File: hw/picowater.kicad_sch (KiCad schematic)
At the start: 45 parts, among them J1 +12V, J10 Batt TP, J11 Humidity, J12 Ultrasound, J2 Power In, J3 +5V Pins, J4 UART, J5 Power Out, J6 JST-PH2 Bat, J7 GPIO2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

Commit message: [hw] update pcb
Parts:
- removed D2: green, LED_THT:LED_D3.0mm, symbol Device:LED
- removed R3: 330, Resistor_SMD:R_1206_3216Metric_Pad1.30x1.75mm_HandSolder, symbol Device:R_Small
- added D4: LED, LED_SMD:LED_0603_1608Metric_Pad1.05x0.95mm_HandSolder, symbol Device:LED
- added R3: 220, Resistor_SMD:R_0402_1005Metric, symbol Device:R
- BT1: footprint Battery:Battery_Panasonic_CR2032-VS1N_Vertical_CircularHoles -> Lunasys_Library:CR2032_Vertical_TE_1775485-1
- C4, C5: LCSC C88484 -> C2846677
- J6: LCSC (none) -> C295747
- Q1: LCSC C18221467 -> C909746
- SW1: footprint Button_Switch_SMD:SW_Push_SPST_NO_Alps_SKRK -> Button_Switch_THT:SW_PUSH_6mm
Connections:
- net GND: now also D4.1 (K)
- net at U1.1 (GPIO0): now also R3.2
- new net: D4.2 (A), R3.1
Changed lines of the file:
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@@
+    (stroke (width 0) (type default))
+  )
+  (wire (pts (xy 193.04 31.75) (xy 194.31 31.75))
     (stroke (width 0) (type default))
   )
@@
     (stroke (width 0) (type default))
   )
-  (wire (pts (xy 187.96 31.75) (xy 190.5 31.75))
-    (stroke (width 0) (type default))
-  )
   (wire (pts (xy 36.195 148.59) (xy 59.69 148.59))
     (stroke (width 0) (type default))
@@
     (stroke (width 0) (type default))
   )
-  (wire (pts (xy 203.2 31.75) (xy 210.82 31.75))
+  (wire (pts (xy 201.93 31.75) (xy 210.82 31.75))
+    (stroke (width 0) (type default))
+  )
+  (wire (pts (xy 181.61 31.75) (xy 185.42 31.75))
     (stroke (width 0) (type default))
   )
@@
       (effects (font (size 1.27 1.27)))
     )
-    (property "Footprint" "Button_Switch_SMD:SW_Push_SPST_NO_Alps_SKRK" (at 34.925 179.07 0)
+    (property "Footprint" "Button_Switch_THT:SW_PUSH_6mm" (at 34.925 179.07 0)
       (effects (font (size 1.27 1.27)) hide)
     )
@@
     )
   )
-  (symbol (lib_id "Device:R_Small") (at 193.04 31.75 270) (unit 1)
-    (in_bom yes) (on_board yes) (dnp no)
-    (property "Reference" "R3" (at 190.5 35.56 0)
-      (effects (font (size 1.27 1.27)) (justify right))
-    )
-    (property "Value" "330" (at 193.04 36.83 0)
-      (effects (font (size 1.27 1.27)) (justify right))
-    )
-    (property "Footprint" "Resistor_SMD:R_1206_3216Metric_Pad1.30x1.75mm_HandSolder" (at 193.04 31.75 0)
-      (effects (font (size 1.27 1.27)) hide)
-    )
-    (property "Datasheet" "~" (at 193.04 31.75 0)
-      (effects (font (size 1.27 1.27)) hide)
-    )
-    (property "LCSC" "C3018003" (at 193.04 31.75 0)
-      (effects (font (size 1.27 1.27)) hide)
-    )
-    (pin "1")
-    (pin "2")
-    (instances
-      (project "picowater"
-        (path "/6f0795e9-9bd6-4197-b73a-51dca38e6e36"
-          (reference "R3") (unit 1)
-        )
-      )
-      (project "ISA rev7"
-        (path "/d1f04949-fb9b-4268-b5f3-6258a63d79ac"
-          (reference "R4") (unit 1)
-        )
-      )
-    )
-  )
   (symbol (lib_id "Relay:G5Q-1") (at 248.92 125.73 0) (unit 1)
     (in_bom yes) (on_board yes) (dnp no)
@@
       (effects (font (size 1.27 1.27)) (justify left) hide)
     )
-    (property "LCSC" "C18221467" (at 224.79 142.24 0)
+    (property "LCSC" "C909746" (at 224.79 142.24 0)
       (effects (font (size 1.27 1.27)) hide)
     )
@@
     )
   )
-  (symbol (lib_id "Device:LED") (at 199.39 31.75 0) (unit 1)
-    (in_bom yes) (on_board yes) (dnp no)
-    (property "Reference" "D2" (at 200.66 35.56 90)
-      (effects (font (size 1.27 1.27)))
-    )
-    (property "Value" "green" (at 198.12 35.56 90)
-      (effects (font (size 1.27 1.27)))
-    )
-    (property "Footprint" "LED_THT:LED_D3.0mm" (at 199.39 31.75 0)
-      (effects (font (size 1.27 1.27)) hide)
-    )
-    (property "Datasheet" "~" (at 199.39 31.75 0)
-      (effects (font (size 1.27 1.27)) hide)
-    )
-    (pin "1")
-    (pin "2")
-    (instances
-      (project "picowater"
-        (path "/6f0795e9-9bd6-4197-b73a-51dca38e6e36"
-          (reference "D2") (unit 1)
-        )
-      )
-      (project "ISA rev7"
-        (path "/d1f04949-fb9b-4268-b5f3-6258a63d79ac"
-          (reference "D2") (unit 1)
-        )
-      )
-    )
-  )
   (symbol (lib_id "power:+BATT") (at 82.55 85.09 90) (unit 1)
     (in_bom yes) (on_board yes) (dnp no) (fields_autoplaced)
@@
         (path "/6f0795e9-9bd6-4197-b73a-51dca38e6e36"
           (reference "#PWR012") (unit 1)
+        )
+      )
+    )
+  )
+  (symbol (lib_id "Device:LED") (at 189.23 31.75 0) (unit 1)
+    (in_bom yes) (on_board yes) (dnp no) (fields_autoplaced)
+    (property "Reference" "D4" (at 187.6425 38.1 0)
+      (effects (font (size 1.27 1.27)))
+    )
+    (property "Value" "LED" (at 187.6425 35.56 0)
+      (effects (font (size 1.27 1.27)))
+    )
+    (property "Footprint" "LED_SMD:LED_0603_1608Metric_Pad1.05x0.95mm_HandSolder" (at 189.23 31.75 0)
+      (effects (font (size 1.27 1.27)) hide)
+    )
+    (property "Datasheet" "~" (at 189.23 31.75 0)
+      (effects (font (size 1.27 1.27)) hide)
+    )
+    (property "JLCPCB Part Number" "C72041" (at 189.23 31.75 0)
+      (effects (font (size 1.27 1.27)) hide)
+    )
+    (pin "1")
+    (pin "2")
+    (instances
+      (project "picowater"
+        (path "/6f0795e9-9bd6-4197-b73a-51dca38e6e36"
+          (reference "D4") (unit 1)
         )
       )
@@
         (path "/6f0795e9-9bd6-4197-b73a-51dca38e6e36"
           (reference "D3") (unit 1)
+        )
+      )
+    )
+  )
+  (symbol (lib_id "Device:R") (at 198.12 31.75 90) (unit 1)
+    (in_bom yes) (on_board yes) (dnp no) (fields_autoplaced)
+    (property "Reference" "R3" (at 198.12 25.4 90)
+      (effects (font (size 1.27 1.27)))
+    )
+    (property "Value" "220" (at 198.12 27.94 90)
+      (effects (font (size 1.27 1.27)))
+    )
+    (property "Footprint" "Resistor_SMD:R_0402_1005Metric" (at 198.12 33.528 90)
+      (effects (font (size 1.27 1.27)) hide)
+    )
+    (property "Datasheet" "~" (at 198.12 31.75 0)
+      (effects (font (size 1.27 1.27)) hide)
+    )
+    (property "LCSC" "C2909336" (at 198.12 31.75 0)
+      (effects (font (size 1.27 1.27)) hide)
+    )
+    (pin "1")
+    (pin "2")
+    (instances
+      (project "picowater"
+        (path "/6f0795e9-9bd6-4197-b73a-51dca38e6e36"
+          (reference "R3") (unit 1)
         )
       )
@@
     )
   )
-  (symbol (lib_id "power:GND") (at 187.96 31.75 0) (unit 1)
-    (in_bom yes) (on_board yes) (dnp no)
-    (property "Reference" "#PWR07" (at 187.96 38.1 0)
-      (effects (font (size 1.27 1.27)) hide)
-    )
-    (property "Value" "GND" (at 185.42 35.56 0)
-      (effects (font (size 1.27 1.27)) (justify left))
-    )
-    (property "Footprint" "" (at 187.96 31.75 0)
-      (effects (font (size 1.27 1.27)) hide)
-    )
-    (property "Datasheet" "" (at 187.96 31.75 0)
+  (symbol (lib_id "power:GND") (at 181.61 31.75 0) (unit 1)
+    (in_bom yes) (on_board yes) (dnp no)
+    (property "Reference" "#PWR07" (at 181.61 38.1 0)
+      (effects (font (size 1.27 1.27)) hide)
+    )
+    (property "Value" "GND" (at 179.07 35.56 0)
+      (effects (font (size 1.27 1.27)) (justify left))
+    )
+    (property "Footprint" "" (at 181.61 31.75 0)
+      (effects (font (size 1.27 1.27)) hide)
+    )
+    (property "Datasheet" "" (at 181.61 31.75 0)
       (effects (font (size 1.27 1.27)) hide)
     )
@@
       (effects (font (size 1.27 1.27)) hide)
     )
-    (property "LCSC" "C88484" (at 97.79 62.23 0)
+    (property "LCSC" "C2846677" (at 97.79 62.23 0)
       (effects (font (size 1.27 1.27)) hide)
     )
@@
       (effects (font (size 1.27 1.27)) hide)
     )
+    (property "LCSC" "C295747" (at 45.72 90.805 0)
+      (effects (font (size 1.27 1.27)) hide)
+    )
     (pin "1")
     (pin "2")
@@
       (effects (font (size 1.27 1.27)) (justify left))
     )
-    (property "Footprint" "Battery:Battery_Panasonic_CR2032-VS1N_Vertical_CircularHoles" (at 64.135 94.996 90)
+    (property "Footprint" "Lunasys_Library:CR2032_Vertical_TE_1775485-1" (at 64.135 94.996 90)
       (effects (font (size 1.27 1.27)) hide)
     )
@@
       (effects (font (size 1.27 1.27)) hide)
     )
-    (property "LCSC" "C88484" (at 116.84 62.23 0)
-      (effects (font (size 1.27 1.27)) hide)
-    )
+    (property "LCSC" "C2846677" (at 116.84 62.23 0)
+      (effects (font (size 1.27 1.27)) hide)
+    )

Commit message: [pcb] fixes
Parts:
- removed Q1: S8050, Package_TO_SOT_SMD:TSOT-23, symbol Transistor_BJT:S8050
- added Q2: BC817, Package_TO_SOT_SMD:SOT-23, symbol Transistor_BJT:BC817
- R10: value 100 -> 220; LCSC C2906884 -> C2909336
- R3: value 220 -> 4.7K; LCSC C2909336 -> (none)
- R7: footprint Resistor_SMD:R_0402_1005Metric -> Resistor_SMD:R_0805_2012Metric
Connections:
- net GND: now also Q2.2 (E)
- net at D3.1 (K), K1.1: now also Q2.3 (C)
- net at R9.2: now also Q2.1 (B)
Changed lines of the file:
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@@
-    )
-  )
-  (symbol (lib_id "Transistor_BJT:S8050") (at 224.79 142.24 0) (unit 1)
-    (in_bom yes) (on_board yes) (dnp no) (fields_autoplaced)
-    (property "Reference" "Q1" (at 229.87 140.97 0)
-      (effects (font (size 1.27 1.27)) (justify left))
-    )
-    (property "Value" "S8050" (at 229.87 143.51 0)
-      (effects (font (size 1.27 1.27)) (justify left))
-    )
-    (property "Footprint" "Package_TO_SOT_SMD:TSOT-23" (at 229.87 144.145 0)
-      (effects (font (size 1.27 1.27) italic) (justify left) hide)
-    )
-    (property "Datasheet" "http://www.unisonic.com.tw/datasheet/S8050.pdf" (at 224.79 142.24 0)
-      (effects (font (size 1.27 1.27)) (justify left) hide)
-    )
-    (property "LCSC" "C909746" (at 224.79 142.24 0)
-      (effects (font (size 1.27 1.27)) hide)
-    )
-    (pin "1")
-    (pin "3")
-    (pin "2")
-    (instances
-      (project "picowater"
-        (path "/6f0795e9-9bd6-4197-b73a-51dca38e6e36"
-          (reference "Q1") (unit 1)
-        )
-      )
     )
   )
@@
       (effects (font (size 1.27 1.27)))
     )
-    (property "Value" "220" (at 198.12 27.94 90)
+    (property "Value" "4.7K" (at 198.12 27.94 90)
       (effects (font (size 1.27 1.27)))
     )
@@
       (effects (font (size 1.27 1.27)) hide)
     )
-    (property "LCSC" "C2909336" (at 198.12 31.75 0)
+    (property "LCSC" "" (at 198.12 31.75 0)
       (effects (font (size 1.27 1.27)) hide)
     )
@@
       (effects (font (size 1.27 1.27)) (justify left))
     )
-    (property "Footprint" "Resistor_SMD:R_0402_1005Metric" (at 121.92 177.292 90)
+    (property "Footprint" "Resistor_SMD:R_0805_2012Metric" (at 121.92 177.292 90)
       (effects (font (size 1.27 1.27)) hide)
     )
@@
         (path "/6f0795e9-9bd6-4197-b73a-51dca38e6e36"
           (reference "#FLG03") (unit 1)
+        )
+      )
+    )
+  )
+  (symbol (lib_id "Transistor_BJT:BC817") (at 224.79 142.24 0) (unit 1)
+    (in_bom yes) (on_board yes) (dnp no) (fields_autoplaced)
+    (property "Reference" "Q2" (at 229.87 140.97 0)
+      (effects (font (size 1.27 1.27)) (justify left))
+    )
+    (property "Value" "BC817" (at 229.87 143.51 0)
+      (effects (font (size 1.27 1.27)) (justify left))
+    )
+    (property "Footprint" "Package_TO_SOT_SMD:SOT-23" (at 229.87 144.145 0)
+      (effects (font (size 1.27 1.27) italic) (justify left) hide)
+    )
+    (property "Datasheet" "https://www.onsemi.com/pub/Collateral/BC818-D.pdf" (at 224.79 142.24 0)
+      (effects (font (size 1.27 1.27)) (justify left) hide)
+    )
+    (pin "2")
+    (pin "3")
+    (pin "1")
+    (instances
+      (project "picowater"
+        (path "/6f0795e9-9bd6-4197-b73a-51dca38e6e36"
+          (reference "Q2") (unit 1)
         )
       )
@@
       (effects (font (size 1.27 1.27)))
     )
-    (property "Value" "100" (at 193.04 120.65 90)
+    (property "Value" "220" (at 193.04 120.65 90)
       (effects (font (size 1.27 1.27)))
     )
@@
       (effects (font (size 1.27 1.27)) hide)
     )
-    (property "LCSC" "C2906884" (at 193.04 123.19 0)
-      (effects (font (size 1.27 1.27)) hide)
-    )
+    (property "LCSC" "C2909336" (at 193.04 123.19 0)
+      (effects (font (size 1.27 1.27)) hide)
+    )
+    (property "Field5" "" (at 193.04 123.19 90)
+      (effects (font (size 1.27 1.27)) hide)
+    )

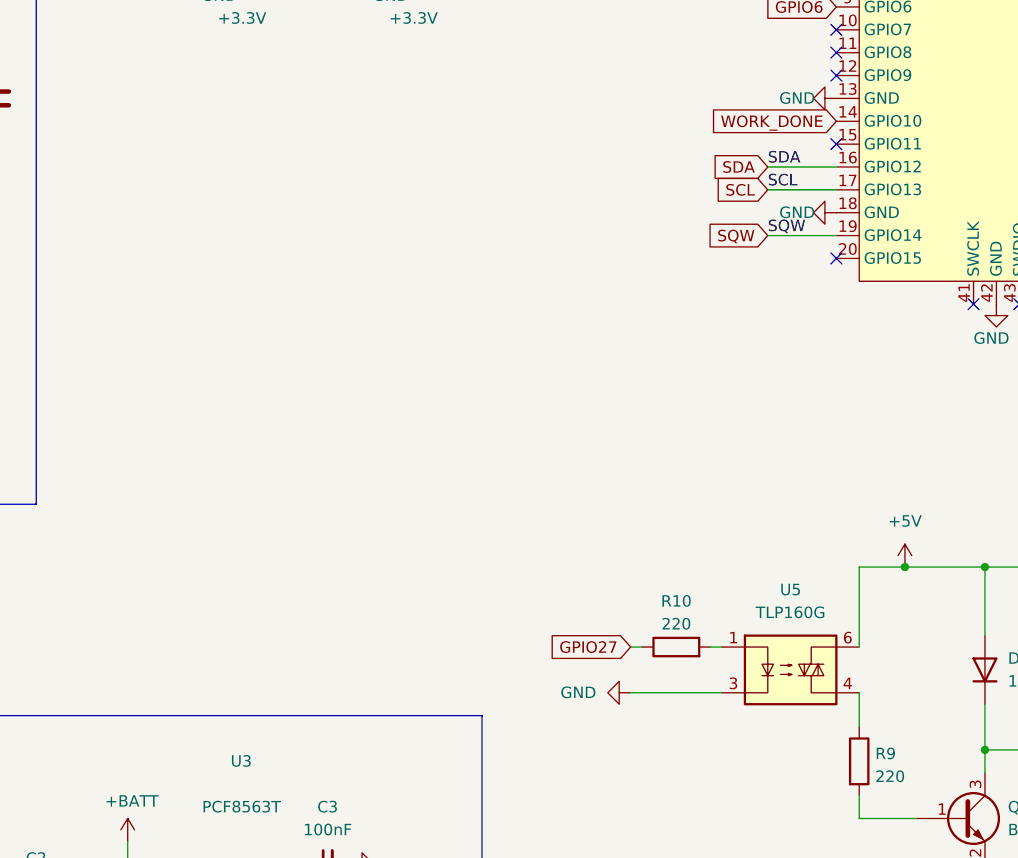
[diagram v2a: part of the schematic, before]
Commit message: better use of the new rtc
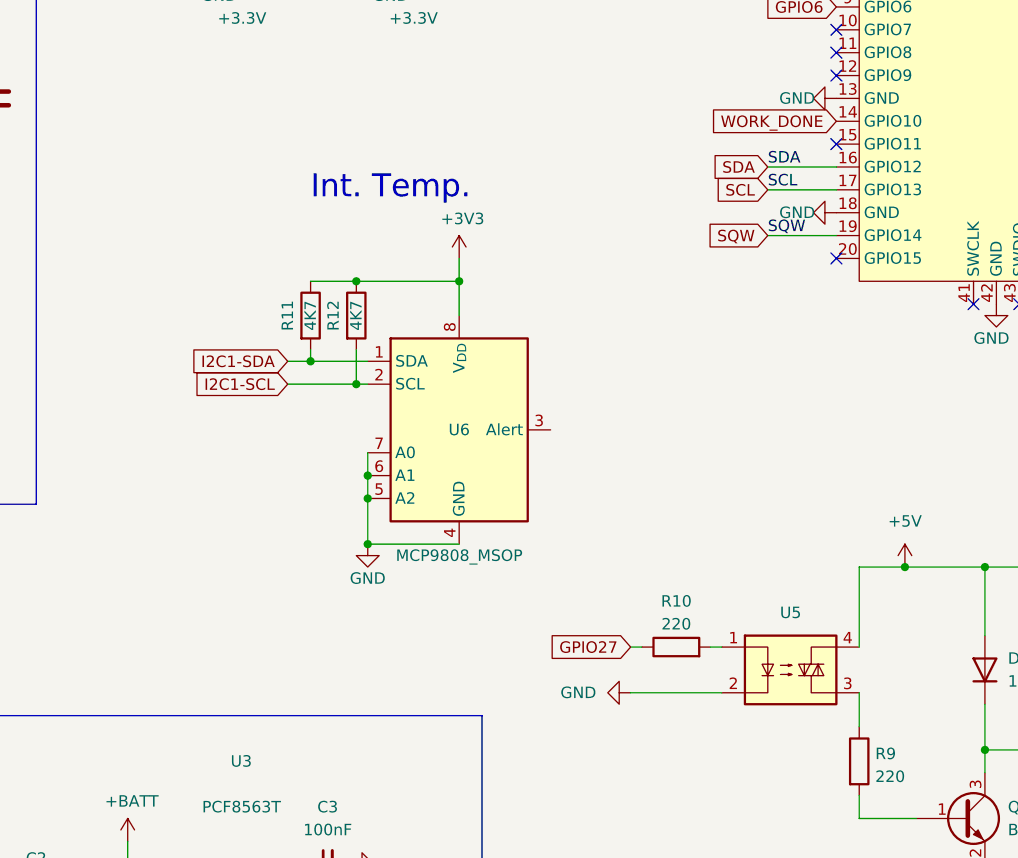
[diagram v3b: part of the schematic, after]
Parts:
- added R11, R12: 4K7, Capacitor_SMD:C_0402_1005Metric, symbol Device:R
- added U6: MCP9808_MSOP, Package_SO:MSOP-8_3x3mm_P0.65mm, symbol Sensor_Temperature:MCP9808_MSOP
- U2: footprint Package_SO:SOIC-14_3.9x8.7mm_P1.27mm -> Package_SO:SO-14_5.3x10.2mm_P1.27mm
- U5: value TLP160G -> ~; footprint Package_SO:MFSOP6-4_4.4x3.6mm_P1.27mm -> Package_DIP:SMDIP-4_W7.62mm; symbol Relay_SolidState:TLP160G -> Relay_SolidState:FODM3011
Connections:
- net +5V: now also U5.4; no longer U5.6
- net GND: now also U5.2, U6.4 (GND), U6.5 (A2), U6.6 (A1), U6.7 (A0); no longer U5.3
- net at R9.1: now also U5.3; no longer U5.4
- new net +3V3: R11.1, R12.1, U6.8 (V_{DD})
- new net I2C1-SCL: R12.2, U6.2 (SCL)
- new net I2C1-SDA: R11.2, U6.1 (SDA)
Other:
- note added: "Int. Temp."
